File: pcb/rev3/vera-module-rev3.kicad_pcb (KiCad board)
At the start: 2 copper layers, 96.5 x 55 mm, 120 parts, among them J1 Bus, J2 Prog, J3 SD_Card, J4 Composite, J5 VGA, J6 Conn_01x04, J7 Conn_01x02, J8 RS232, J9 S-video, U1 ICE40UP5K-SG48ITR50, U10 MIC5504-3.3YM5, U11 THS7314D, U12 MAX3221CPWR, U2 74AHC00PW, U3 SN74CBTD3861PWR, U4 74AHC1G14GW,125, U5 74LVC4245APW, U6 WM8524CGEDT, U7 W25Q16JVSNIQ, U8 74AHC1G14GW,125, U9 AP3417CKTR-G1, X1 SG5032CAN_25.000000M-TJGA3

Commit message: Worked on rev3 PCB.
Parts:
- removed C27, C28, C29, C31, C32, C36: 100nF, Capacitor_SMD:C_0603_1608Metric
- removed J6: Conn_01x04, Connector_PinHeader_2.54mm:PinHeader_1x04_P2.54mm_Vertical
- removed J7: Conn_01x02, Connector_PinHeader_2.54mm:PinHeader_1x02_P2.54mm_Vertical
- removed J8: RS232, Connector_PinHeader_2.54mm:PinHeader_2x05_P2.54mm_Vertical
- removed U12: MAX3221CPWR, Package_SO:TSSOP-16_4.4x5mm_P0.65mm
- removed U4, U8: 74AHC1G14GW,125, Package_TO_SOT_SMD:SOT-353_SC-70-5
- added JP1: Flash enable, Connector_PinHeader_2.54mm:PinHeader_1x02_P2.54mm_Vertical, F.Cu at (131.0, 123.0)
- J1: footprint Connector_PinHeader_2.54mm:PinHeader_2x11_P2.54mm_Vertical -> Connector_PinHeader_2.54mm:PinHeader_2x12_P2.54mm_Vertical
- moved J1 2.54 mm to (160.0, 133.0)
- moved C25 1.55 mm to (155.1, 130.7)
- moved C26 1.55 mm to (155.1, 124.8)
- moved R18 1.55 mm to (155.1, 132.4)
- moved U10 1.55 mm to (155.1, 127.7)
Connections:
- J1 pad 13: BUS_RW#_5V -> BUS_WR#_5V
- J1 pad 15: BUS_A2_5V -> BUS_A4_5V
- J1 pad 16: BUS_A1_5V -> BUS_RD#_5V
- J1 pad 17: BUS_A0_5V -> BUS_A2_5V
- J1 pad 18: BUS_PHI2_5V -> BUS_A3_5V
- J1 pad 19: GND -> BUS_A0_5V
- J1 pad 20: GND -> BUS_A1_5V
- J1 pad 21: L_AUDIO -> GND
- J1 pad 22: R_AUDIO -> GND
- U1 pad 31: BUS_RW# -> BUS_WR#
- U1 pad 34: UART_RX -> BUS_A4
- U1 pad 36: UART_TX -> BUS_RD#
- U1 pad 37: BUS_PHI2 -> BUS_A2
- U1 pad 39: BUS_A2 -> BUS_A1
- U1 pad 40: BUS_A1 -> BUS_A0
- U1 pad 41: BUS_A0 -> BUS_A3
- U3 pad 10: BUS_CS# -> FPGA_CRESET_B
- U3 pad 11: GND -> BUS_CS#
- U3 pad 13: (no net) -> BUS_CS#_5V
- U3 pad 14: BUS_CS#_5V -> BUS_RES#_5V
- U3 pad 15: BUS_RES#_5V -> BUS_WR#_5V
- U3 pad 16: BUS_RW#_5V -> BUS_IRQ#_5V
- U3 pad 17: BUS_IRQ#_5V -> BUS_A4_5V
- U3 pad 18: BUS_A2_5V -> BUS_RD#_5V
- U3 pad 19: BUS_A1_5V -> BUS_A2_5V
- U3 pad 2: GND -> BUS_A1
- U3 pad 20: BUS_A0_5V -> BUS_A3_5V
- U3 pad 21: (no net) -> BUS_A0_5V
- U3 pad 22: (no net) -> BUS_A1_5V
- U3 pad 3: GND -> BUS_A0
- U3 pad 4: BUS_A0 -> BUS_A3
- U3 pad 5: BUS_A1 -> BUS_A2
- U3 pad 6: BUS_A2 -> BUS_RD#
- U3 pad 7: BUS_IRQ# -> BUS_A4
- U3 pad 8: BUS_RW# -> BUS_IRQ#
- U3 pad 9: FPGA_CRESET_B -> BUS_WR#
- U5 pad 2: Net-(U4-Pad4) -> BUS_RD#_5V
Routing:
- net UART_TX: track 80.6 -> 0.00 mm, vias 4 -> 0
- net UART_RX: track 77.0 -> 0.00 mm, vias 2 -> 0
- net +5V: track 120.3 -> 74.0 mm, vias 8 -> 2
- net +3V3: track 267.4 -> 241.0 mm
- net BUS_RW#_5V: track 25.2 -> 0.00 mm
- net BUS_A3: track 0.00 -> 20.3 mm, vias 0 -> 2
- net FPGA_CDONE: track 55.9 -> 75.4 mm, vias 4 -> 6
- net BUS_RD#_5V: track 0.00 -> 17.6 mm
- net Net-(J7-Pad1): track 16.2 -> 0.00 mm
- net Net-(J7-Pad2): track 15.2 -> 0.00 mm
- net BUS_PHI2: track 12.7 -> 0.00 mm, vias 2 -> 0
- net BUS_A4: track 0.00 -> 12.2 mm
- net GND: track 66.8 -> 54.8 mm, vias 159 -> 154
- net Net-(J8-Pad5): track 11.7 -> 0.00 mm
- net BUS_RD#: track 0.00 -> 11.5 mm, vias 0 -> 2
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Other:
- board text removed: "5V"
- board text removed: "GND"
- board text removed: "RS232"
- board text removed: "RX"
- board text removed: "TX"

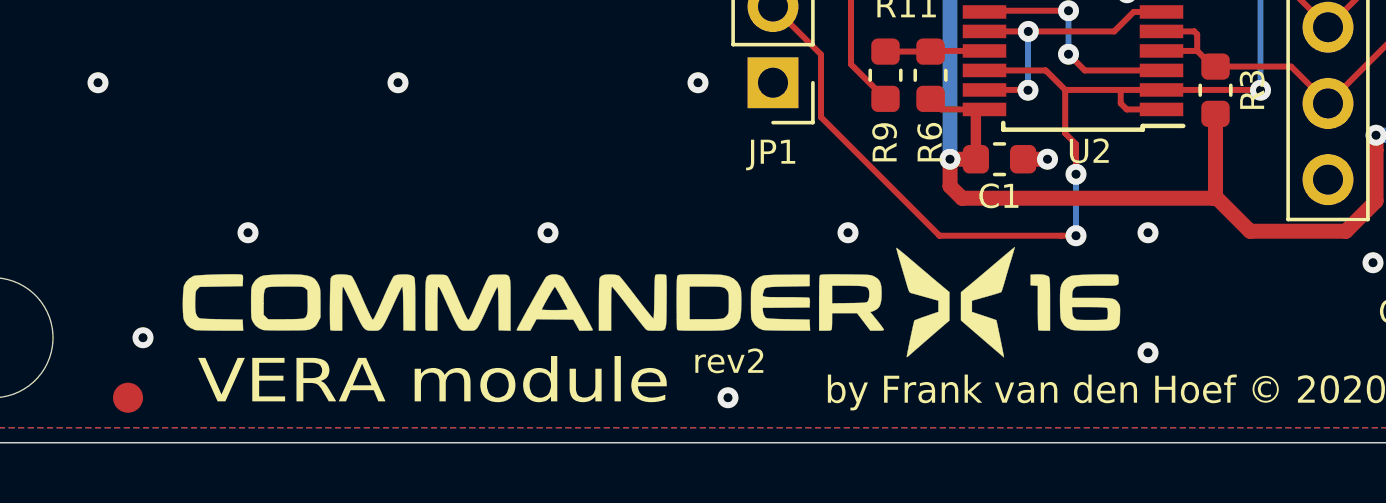
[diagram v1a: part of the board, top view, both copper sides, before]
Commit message: Adding address decrement. Fixing port 1 address increment.
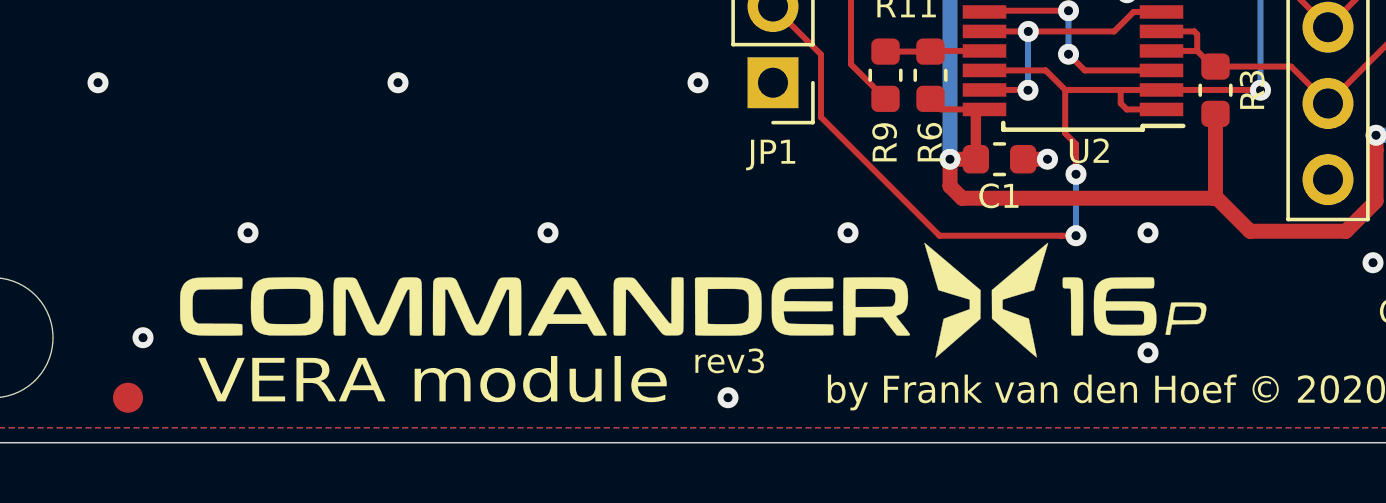
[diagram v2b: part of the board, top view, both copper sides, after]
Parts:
- LOGO1: footprint vera-module:x16logo -> vera-module:x16plogo
- moved LOGO1 1.35 mm to (128.3, 130.3)
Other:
- board text added: "rev3"
- board text removed: "rev2"
